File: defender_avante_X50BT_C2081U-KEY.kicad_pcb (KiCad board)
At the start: 2 copper layers, 172.7 x 61 mm, 86 parts, among them CN301 CONNECTOR_M_006_20_SPECIAL, J300 JUMPER, J301 JUMPER, J302 JUMPER, J303 JUMPER, J304 JUMPER, J305 JUMPER, J306 JUMPER, J307 JUMPER, J308 JUMPER, J309 JUMPER, J310 JUMPER, J311 JUMPER, J312 JUMPER, J313 JUMPER, J314 JUMPER, J315 JUMPER, J316 JUMPER, J317 JUMPER, J318 JUMPER, J319 JUMPER, J320 JUMPER, J321 JUMPER, J322 JUMPER, J323 JUMPER, J324 JUMPER, J325 JUMPER, J326 JUMPER, J327 JUMPER, J328 JUMPER, J329 JUMPER, J330 JUMPER, J331 JUMPER, J332 JUMPER, J333 JUMPER, J334 JUMPER, J335 JUMPER, J336 JUMPER, Q300 BJT_NPN_GENERAL, U300 TM1668

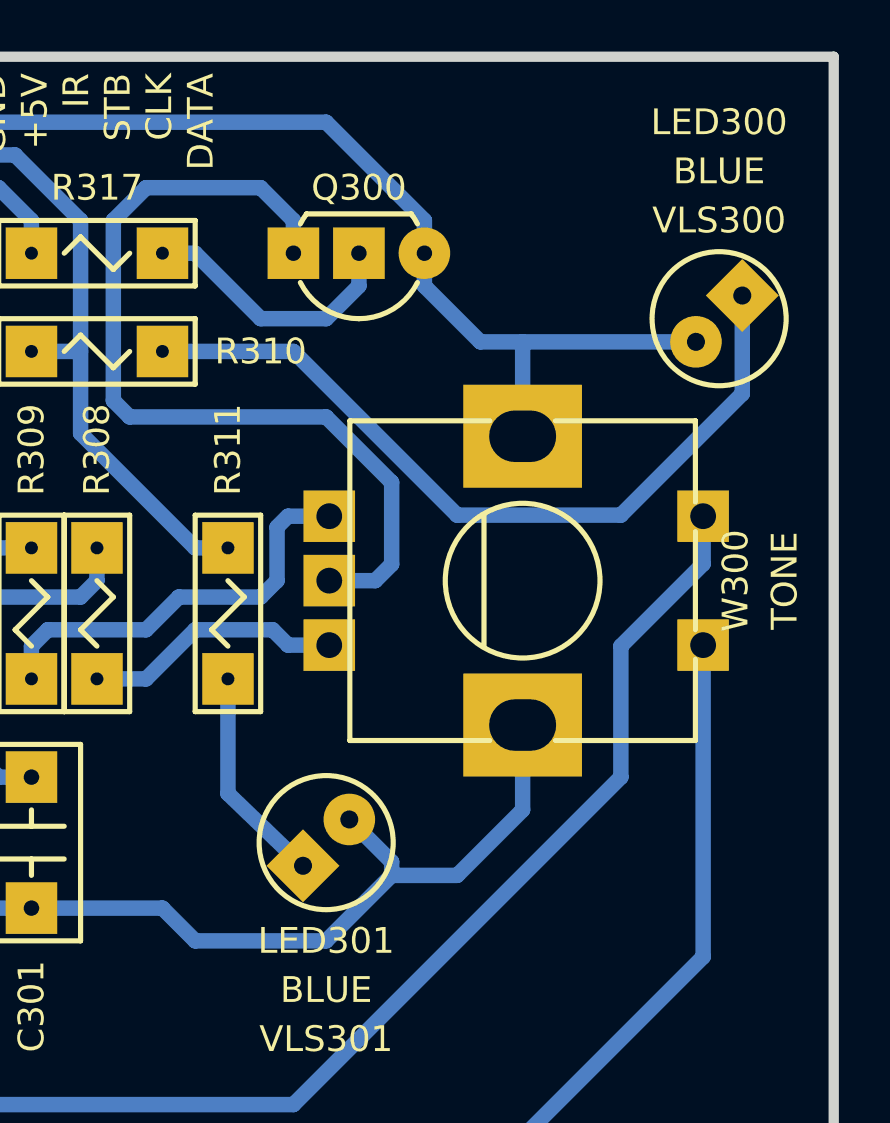
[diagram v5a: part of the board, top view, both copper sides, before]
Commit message: Повёрнуты светодиоды. Залочены футпринты энкодера и разъёма
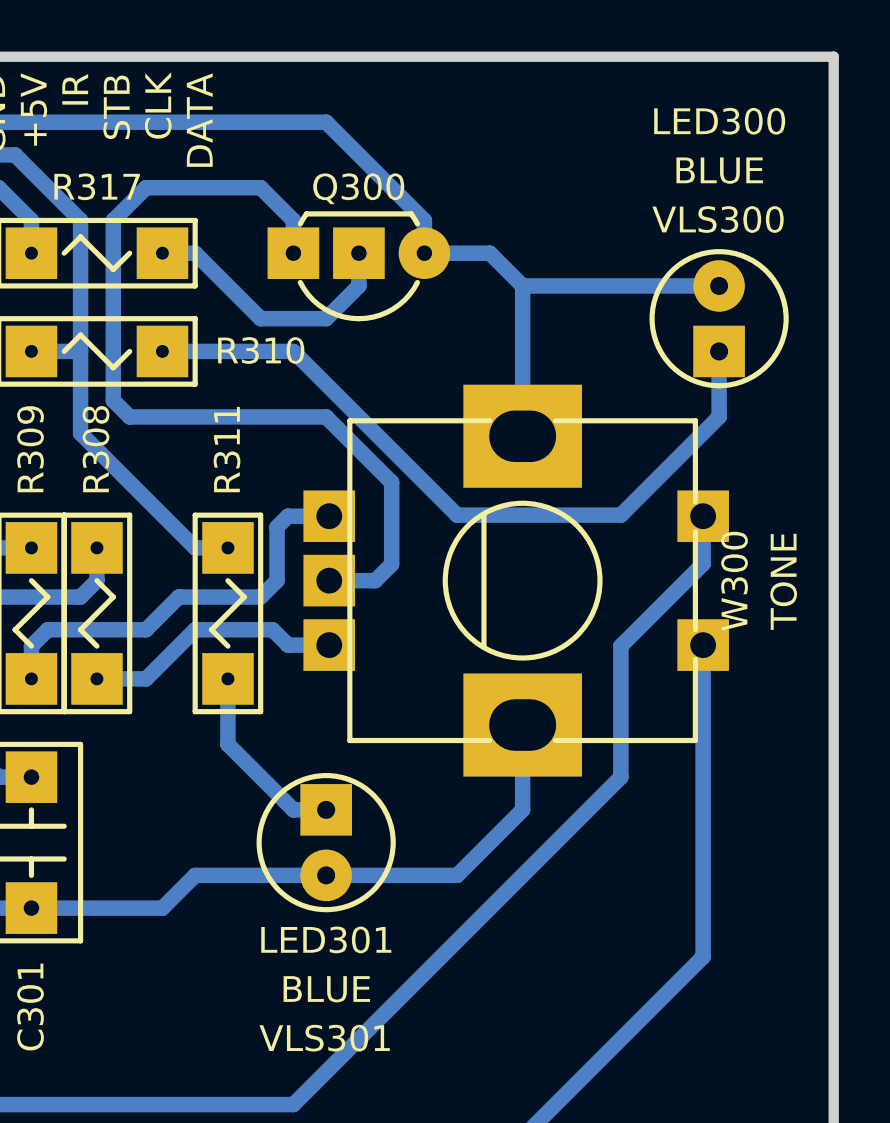
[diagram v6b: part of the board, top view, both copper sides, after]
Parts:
- turned LED300 to 270 degrees
- turned LED301 to 90 degrees
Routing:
- net Net-(LED300-PadA): track 30.9 -> 28.3 mm
- net COM: track 324.2 -> 321.7 mm
- net Net-(LED301-PadA): track 8.49 -> 7.40 mm
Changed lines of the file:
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@@
-(kicad_pcb (version 20171130) (host pcbnew 5.0.2-bee76a0~70~ubuntu18.04.1)
+(kicad_pcb (version 20171130) (host pcbnew 5.1.4-e60b266~84~ubuntu18.04.1)
   (general
     (thickness 1.5)
     (drawings 21)
-    (tracks 502)
+    (tracks 500)
     (zones 0)
     (modules 86)
@@
   (title_block
     (title defender_avante_X50BT_C2081U-KEY)
-    (date 2019-06-04)
+    (date 2019-09-02)
     (rev 2)
     (company "Igor Vladimirovich Ivanov")
@@
     (zone_45_only no)
     (trace_min 0.2)
-    (segment_width 0.2)
-    (edge_width 0.4)
     (via_size 3)
     (via_drill 1)
@@
     (uvia_min_size 0)
     (uvia_min_drill 0)
+    (edge_width 0.4)
+    (segment_width 0.2)
     (pcb_text_width 0.3)
     (pcb_text_size 1.5 1.5)
@@
       (net 35 /IR))
   )
-  (module KCL:CON-CWF-6RA (layer F.Cu)
+  (module KCL:CON-CWF-6RA locked (layer F.Cu)
     (at 191.77 82.55)
     (fp_text reference CN301 (at 0 1.27) (layer F.SilkS)
@@
   )
   (module KCL:LED-ROUND-03.0-UNI-SH-SPACER locked (layer F.Cu)
-    (at 229.87 85.09 45)
-    (fp_text reference LED300 (at 5.388154 -5.388154 180) (layer F.SilkS)
+    (at 229.87 85.09 270)
+    (fp_text reference LED300 (at -7.62 0) (layer F.SilkS)
       (effects (font (size 1 1) (thickness 0.2)))
     )
-    (fp_text value DIODE_LIGHT-EMITTING_LEFT (at 10.776307 10.776307 180) (layer F.Fab) hide
+    (fp_text value DIODE_LIGHT-EMITTING_LEFT (at 0 -15.24) (layer F.Fab) hide
       (effects (font (size 1 1) (thickness 0.2)))
     )
     (fp_line (start -0.556776 -1.5) (end 0.556776 -1.5) (layer F.Fab) (width 0.2))
     (fp_arc (start 0 0) (end -0.556776 -1.5) (angle -319.3) (layer F.Fab) (width 0.2))
-    (pad A thru_hole rect (at 1.270001 0 45) (size 2 2) (drill 0.7) (layers B.Cu B.Mask)
+    (pad A thru_hole rect (at 1.270001 0 270) (size 2 2) (drill 0.7) (layers B.Cu B.Mask)
       (net 5 "Net-(LED300-PadA)"))
-    (pad C thru_hole circle (at -1.270001 0 45) (size 2 2) (drill 0.7) (layers B.Cu B.Mask)
+    (pad C thru_hole circle (at -1.270001 0 270) (size 2 2) (drill 0.7) (layers B.Cu B.Mask)
       (net 40 COM))
   )
   (module KCL:LED-ROUND-03.0-UNI-SH-SPACER locked (layer F.Cu)
-    (at 214.63 105.41 225)
-    (fp_text reference LED301 (at 2.694077 -2.694077) (layer F.SilkS)
+    (at 214.63 105.41 90)
+    (fp_text reference LED301 (at -3.81 0 180) (layer F.SilkS)
       (effects (font (size 1 1) (thickness 0.2)))
     )
-    (fp_text value DIODE_LIGHT-EMITTING_LEFT (at -21.552615 -21.552615) (layer F.Fab) hide
+    (fp_text value DIODE_LIGHT-EMITTING_LEFT (at 0 30.48 180) (layer F.Fab) hide
       (effects (font (size 1 1) (thickness 0.2)))
     )
     (fp_line (start -0.556776 -1.5) (end 0.556776 -1.5) (layer F.Fab) (width 0.2))
     (fp_arc (start 0 0) (end -0.556776 -1.5) (angle -319.3) (layer F.Fab) (width 0.2))
-    (pad A thru_hole rect (at 1.270001 0 225) (size 2 2) (drill 0.7) (layers B.Cu B.Mask)
+    (pad A thru_hole rect (at 1.270001 0 90) (size 2 2) (drill 0.7) (layers B.Cu B.Mask)
       (net 6 "Net-(LED301-PadA)"))
-    (pad C thru_hole circle (at -1.270001 0 225) (size 2 2) (drill 0.7) (layers B.Cu B.Mask)
+    (pad C thru_hole circle (at -1.270001 0 90) (size 2 2) (drill 0.7) (layers B.Cu B.Mask)
       (net 40 COM))
   )
@@
       (net 27 "Net-(D303-PadC)"))
   )
-  (module KCL:ENC-PEC12R-4-F-S (layer F.Cu)
+  (module KCL:ENC-PEC12R-4-F-S locked (layer F.Cu)
     (at 222.25 95.25 270)
     (fp_text reference W300 (at 0 -8.255 90) (layer F.SilkS)
@@
   (segment (start 213.15 97.75) (end 212.555 97.155) (width 0.6) (layer B.Cu) (net 4))
   (segment (start 214.75 97.75) (end 213.15 97.75) (width 0.6) (layer B.Cu) (net 4))
+  (segment (start 229.87 88.9) (end 229.87 86.36) (width 0.6) (layer B.Cu) (net 5))
+  (segment (start 226.06 92.71) (end 229.87 88.9) (width 0.6) (layer B.Cu) (net 5))
   (segment (start 219.71 92.71) (end 226.06 92.71) (width 0.6) (layer B.Cu) (net 5))
   (segment (start 208.28 86.36) (end 213.36 86.36) (width 0.6) (layer B.Cu) (net 5))
   (segment (start 213.36 86.36) (end 219.71 92.71) (width 0.6) (layer B.Cu) (net 5))
-  (segment (start 230.768026 88.001974) (end 230.768026 84.191974) (width 0.6) (layer B.Cu) (net 5))
-  (segment (start 226.06 92.71) (end 230.768026 88.001974) (width 0.6) (layer B.Cu) (net 5))
-  (segment (start 210.82 103.505) (end 213.731974 106.308026) (width 0.6) (layer B.Cu) (net 6))
-  (segment (start 210.82 99.06) (end 210.82 103.505) (width 0.6) (layer B.Cu) (net 6))
+  (segment (start 210.82 99.06) (end 210.82 101.6) (width 0.6) (layer B.Cu) (net 6))
+  (segment (start 213.36 104.14) (end 214.63 104.14) (width 0.6) (layer B.Cu) (net 6))
+  (segment (start 210.82 101.6) (end 213.36 104.14) (width 0.6) (layer B.Cu) (net 6))
   (segment (start 180.34 107.95) (end 182.88 107.95) (width 0.6) (layer B.Cu) (net 7))
   (segment (start 180.34 99.06) (end 180.34 107.95) (width 0.6) (layer B.Cu) (net 7))
@@
   (segment (start 194.31 107.95) (end 198.12 107.95) (width 0.6) (layer B.Cu) (net 40))
   (segment (start 198.12 107.95) (end 203.2 107.95) (width 0.6) (layer B.Cu) (net 40))
-  (segment (start 222.25 89.65) (end 222.25 85.988026) (width 0.6) (layer B.Cu) (net 40))
-  (segment (start 222.25 104.14) (end 222.25 100.85) (width 0.6) (layer B.Cu) (net 40))
-  (segment (start 203.2 107.95) (end 208.28 107.95) (width 0.6) (layer B.Cu) (net 40))
-  (segment (start 208.28 107.95) (end 209.55 109.22) (width 0.6) (layer B.Cu) (net 40))
-  (segment (start 220.608026 85.988026) (end 228.971974 85.988026) (width 0.6) (layer B.Cu) (net 40))
-  (segment (start 218.44 82.55) (end 218.44 83.82) (width 0.6) (layer B.Cu) (net 40))
-  (segment (start 218.44 83.82) (end 220.608026 85.988026) (width 0.6) (layer B.Cu) (net 40))
-  (segment (start 217.17 106.153948) (end 215.528026 104.511974) (width 0.6) (layer B.Cu) (net 40))
-  (segment (start 214.63 109.22) (end 217.17 106.68) (width 0.6) (layer B.Cu) (net 40))
-  (segment (start 217.17 106.68) (end 217.17 106.153948) (width 0.6) (layer B.Cu) (net 40))
-  (segment (start 209.55 109.22) (end 214.63 109.22) (width 0.6) (layer B.Cu) (net 40))
-  (segment (start 217.17 106.68) (end 219.71 106.68) (width 0.6) (layer B.Cu) (net 40))
-  (segment (start 219.71 106.68) (end 222.25 104.14) (width 0.6) (layer B.Cu) (net 40))
   (segment (start 218.44 81.28) (end 214.63 77.47) (width 0.6) (layer B.Cu) (net 40))
   (segment (start 218.44 82.55) (end 218.44 81.28) (width 0.6) (layer B.Cu) (net 40))
@@
   (segment (start 214.63 77.47) (end 189.33 77.47) (width 0.6) (layer B.Cu) (net 40))
   (segment (start 189.33 77.47) (end 185.52 81.28) (width 0.6) (layer B.Cu) (net 40))
-  (segment (start 132.08 89.535) (end 127.635 85.09) (width 0.6) (layer B.Cu) (net 42))
-  (segment (start 132.08 101.6) (end 132.08 89.535) (width 0.6) (layer B.Cu) (net 42))
-  (segment (start 124.94 106.68) (end 127 106.68) (width 0.6) (layer B.Cu) (net 42))
-  (segment (start 127 106.68) (end 132.08 101.6) (width 0.6) (layer B.Cu) (net 42))
-  (segment (start 120.65 85.09) (end 127.635 85.09) (width 0.6) (layer B.Cu) (net 42))
+  (segment (start 209.55 106.68) (end 214.63 106.68) (width 0.6) (layer B.Cu) (net 40))
+  (segment (start 203.2 107.95) (end 208.28 107.95) (width 0.6) (layer B.Cu) (net 40))
+  (segment (start 208.28 107.95) (end 209.55 106.68) (width 0.6) (layer B.Cu) (net 40))
+  (segment (start 222.25 104.14) (end 222.25 100.85) (width 0.6) (layer B.Cu) (net 40))
+  (segment (start 214.63 106.68) (end 219.71 106.68) (width 0.6) (layer B.Cu) (net 40))
+  (segment (start 219.71 106.68) (end 222.25 104.14) (width 0.6) (layer B.Cu) (net 40))
+  (segment (start 222.25 83.82) (end 222.25 89.65) (width 0.6) (layer B.Cu) (net 40))
+  (segment (start 220.98 82.55) (end 222.25 83.82) (width 0.6) (layer B.Cu) (net 40))
+  (segment (start 218.44 82.55) (end 220.98 82.55) (width 0.6) (layer B.Cu) (net 40))
+  (segment (start 222.25 83.82) (end 229.87 83.82) (width 0.6) (layer B.Cu) (net 40))
   (segment (start 126.365 105.41) (end 130.81 100.965) (width 0.6) (layer B.Cu) (net 41))
   (segment (start 126.365 105.41) (end 124.94 105.41) (width 0.6) (layer B.Cu) (net 41))
@@
   (segment (start 128.27 87.63) (end 130.81 90.17) (width 0.6) (layer B.Cu) (net 41))
   (segment (start 128.27 87.63) (end 115.57 87.63) (width 0.6) (layer B.Cu) (net 41))
+  (segment (start 132.08 89.535) (end 127.635 85.09) (width 0.6) (layer B.Cu) (net 42))
+  (segment (start 132.08 101.6) (end 132.08 89.535) (width 0.6) (layer B.Cu) (net 42))
+  (segment (start 124.94 106.68) (end 127 106.68) (width 0.6) (layer B.Cu) (net 42))
+  (segment (start 127 106.68) (end 132.08 101.6) (width 0.6) (layer B.Cu) (net 42))
+  (segment (start 120.65 85.09) (end 127.635 85.09) (width 0.6) (layer B.Cu) (net 42))
   (segment (start 132.08 111.76) (end 134.62 111.76) (width 0.6) (layer B.Cu) (net 43))
   (segment (start 134.14 105.41) (end 135.89 105.41) (width 0.6) (layer B.Cu) (net 43))

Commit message: Проект скорректирован с учётом изменений в УГО и ФП переключателей
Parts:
- S300, S301, S302, S303: value SWITCH_BUTTON_NO_01 -> SWITCH_BUTTON_NON-LOCK_01P_01T_NO
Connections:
- U300 pad 15: Net-(U300-Pad15) -> (no net)
- U300 pad 16: Net-(U300-Pad16) -> (no net)
- U300 pad 17: Net-(U300-Pad17) -> (no net)
- U300 pad 18: Net-(U300-Pad18) -> (no net)
- U300 pad 19: Net-(U300-Pad19) -> (no net)
- U300 pad 4: Net-(U300-Pad4) -> (no net)
